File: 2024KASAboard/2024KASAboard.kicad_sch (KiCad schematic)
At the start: 2 parts, among them U1 Pico, U2 BME280

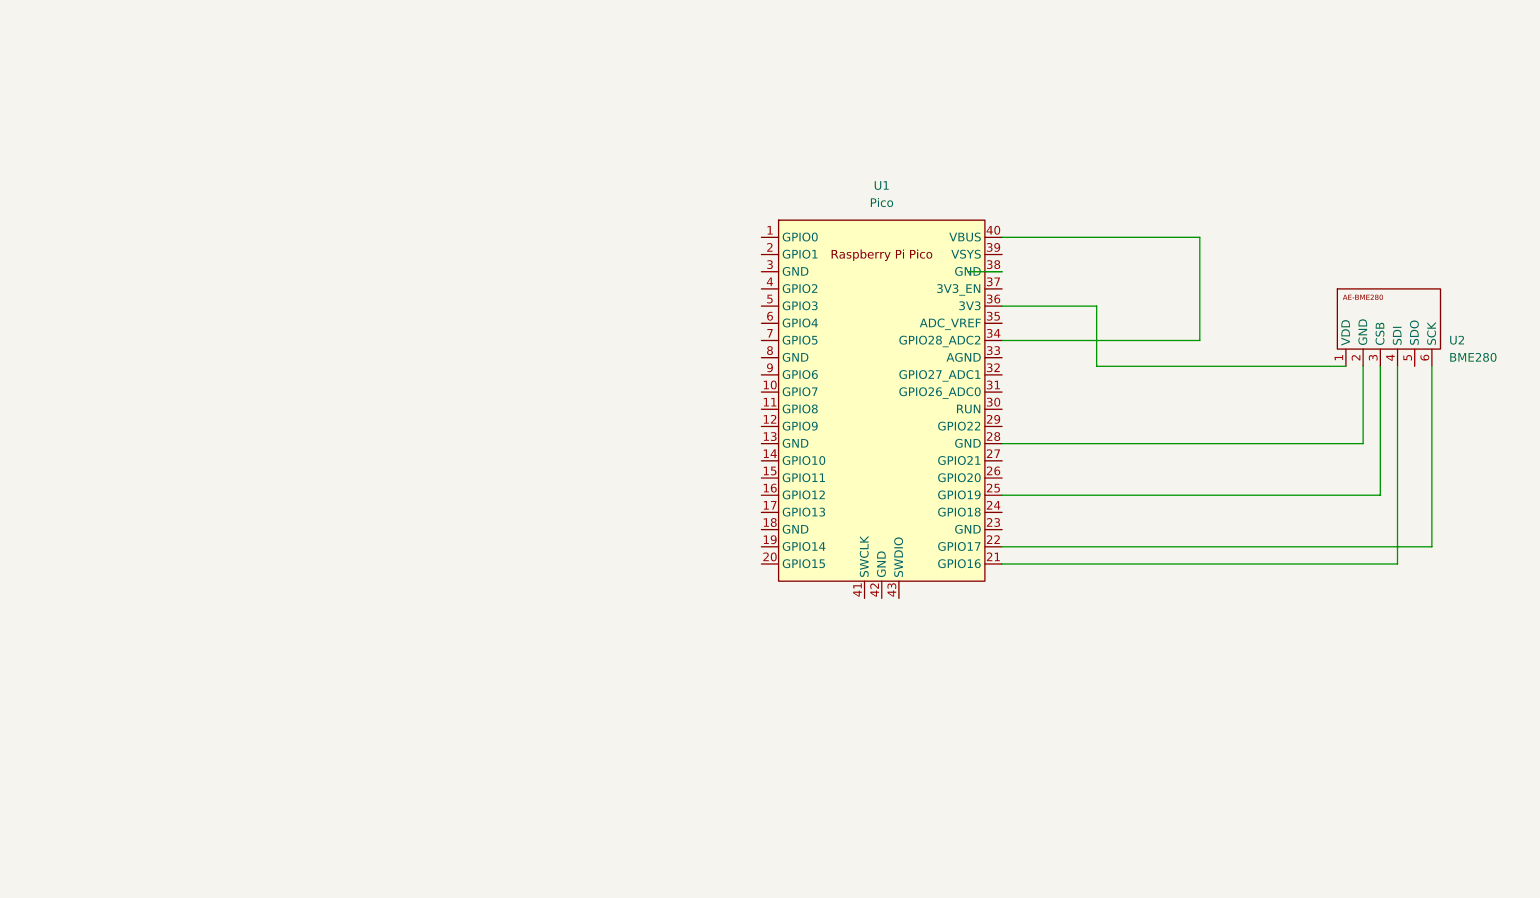
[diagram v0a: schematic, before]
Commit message: boardschcomp
回路図(基本)
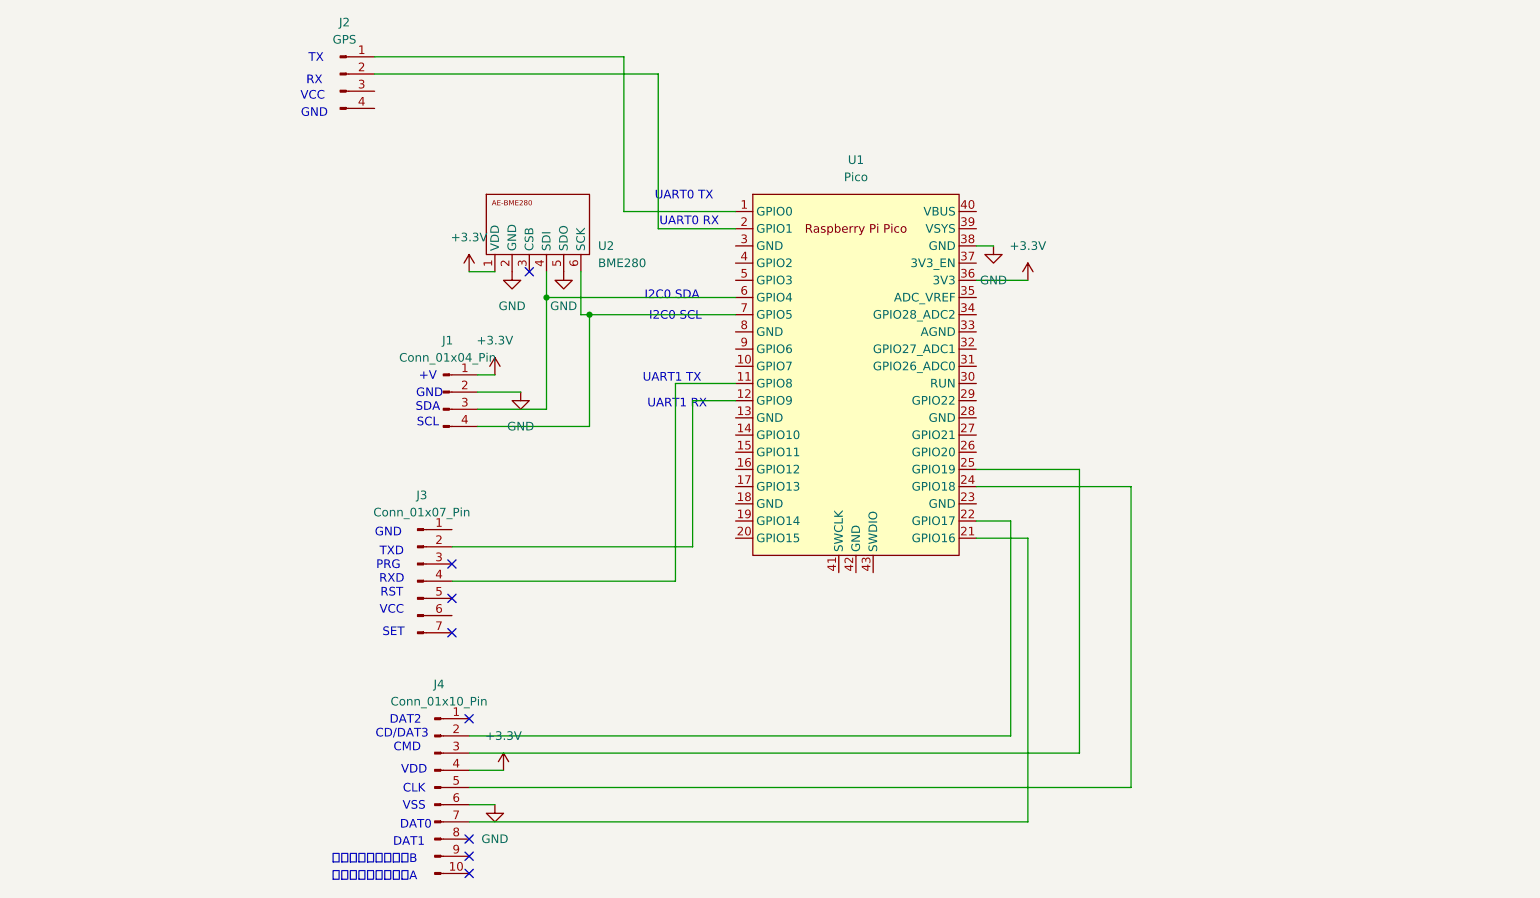
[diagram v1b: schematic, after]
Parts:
- added J1: Conn_01x04_Pin, symbol Connector:Conn_01x04_Pin
- added J2: GPS, symbol Connector:Conn_01x04_Pin
- added J3: Conn_01x07_Pin, symbol Connector:Conn_01x07_Pin
- added J4: Conn_01x10_Pin, symbol Connector:Conn_01x10_Pin
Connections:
- net +3.3V: now reaches U1.36 (3V3), U2.1 (VDD)
- net +3.3V: now also J1.1 (Pin_1), J4.4 (Pin_4)
- net at U1.28 (GND): no longer U2.2 (GND)
- net at U2.3 (CSB): no longer U1.25 (GPIO19)
- net at U2.4 (SDI): now also U1.6 (GPIO4), J1.3 (Pin_3); no longer U1.21 (GPIO16)
- net GND: now reaches U2.5 (SDO)
- net GND: now also U1.38 (GND), U2.2 (GND), J1.2 (Pin_2), J4.6 (Pin_6)
- net at U2.6 (SCK): now also U1.7 (GPIO5), J1.4 (Pin_4); no longer U1.22 (GPIO17)
- net at U1.1 (GPIO0): now also J2.1 (Pin_1)
- net at U1.11 (GPIO8): now also J3.4 (Pin_4)
- net at U1.12 (GPIO9): now also J3.2 (Pin_2)
- net at U1.2 (GPIO1): now also J2.2 (Pin_2)
- net at U1.24 (GPIO18): now also J4.5 (Pin_5)
- net at U1.34 (GPIO28_ADC2): no longer U1.40 (VBUS)
- new net: J4.2 (Pin_2), U1.22 (GPIO17)
- new net: J4.3 (Pin_3), U1.25 (GPIO19)
- new net: J4.7 (Pin_7), U1.21 (GPIO16)
- no-connect marks 0 -> 8
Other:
- note added: "+V"
- note added: "CD/DAT3"
- note added: "CLK"
- note added: "CMD"
- note added: "DAT0"
- note added: "DAT1"
- note added: "DAT2"
- note added: "GND"
- note added: "I2C0 SCL"
- note added: "I2C0 SDA"
- note added: "PRG"
- note added: "RST"
- note added: "RX"
- note added: "RXD"
- note added: "SCL"
- note added: "SDA"
- note added: "SET"
- note added: "TX"
- note added: "TXD"
- note added: "UART0 RX"
- note added: "UART0 TX"
- note added: "UART1 RX"
- note added: "UART1 TX"
- note added: "VCC"
- note added: "VDD"
- note added: "VSS"
- note added: "カード検出スイッチA"
- note added: "カード検出スイッチB"

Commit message: base_sch_addbatt
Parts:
- added BT1: Battery_Cell_NiMH_3.6V, symbol Device:Battery_Cell
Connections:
- net +3.3V: now also BT1.2 (-)
- net at U1.39 (VSYS): now also BT1.1 (+)
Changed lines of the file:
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@@
 	(paper "A4")
+	(junction
+		(at 157.48 66.04)
+		(diameter 0)
+		(color 0 0 0 0)
+	)
 	(junction
 		(at 86.36 68.58)
@@
 	(wire
 		(pts
+			(xy 170.18 64.77) (xy 170.18 66.04)
+		)
+		(stroke
+			(width 0)
+			(type default)
+		)
+	)
+	(wire
+		(pts
 			(xy 76.2 82.55) (xy 82.55 82.55)
 		)
@@
 	(wire
 		(pts
+			(xy 157.48 66.04) (xy 170.18 66.04)
+		)
+		(stroke
+			(width 0)
+			(type default)
+		)
+	)
+	(wire
+		(pts
 			(xy 97.79 33.02) (xy 60.96 33.02)
 		)
@@
 	(wire
 		(pts
+			(xy 170.18 57.15) (xy 149.86 57.15)
+		)
+		(stroke
+			(width 0)
+			(type default)
+		)
+	)
+	(wire
+		(pts
 			(xy 76.2 80.01) (xy 78.74 80.01)
 		)
@@
 		(pts
 			(xy 72.39 110.49) (xy 105.41 110.49)
+		)
+		(stroke
+			(width 0)
+			(type default)
+		)
+	)
+	(wire
+		(pts
+			(xy 149.86 57.15) (xy 149.86 58.42)
 		)
 		(stroke
@@
 					(unit 1)
 				)
+			)
+		)
+	)
+	(symbol
+		(lib_id "Device:Battery_Cell")
+		(at 170.18 62.23 0)
+		(unit 1)
+		(exclude_from_sim no)
+		(in_bom yes)
+		(on_board yes)
+		(dnp no)
+		(fields_autoplaced yes)
+		(property "Reference" "BT1"
+			(at 173.99 59.1184 0)
+			(effects
+				(font
+					(size 1.27 1.27)
+				)
+				(justify left)
+			)
+		)
+		(property "Value" "Battery_Cell_NiMH_3.6V"
+			(at 173.99 61.6584 0)
+			(effects
+				(font
+					(size 1.27 1.27)
+				)
+				(justify left)
+			)
+		)
+		(property "Footprint" ""
+			(at 170.18 60.706 90)
+			(effects
+				(font
+					(size 1.27 1.27)
+				)
+				(hide yes)
+			)
+		)
+		(property "Datasheet" "~"
+			(at 170.18 60.706 90)
+			(effects
+				(font
+					(size 1.27 1.27)
+				)
+				(hide yes)
+			)
+		)
+		(property "Description" "Single-cell battery"
+			(at 170.18 62.23 0)
+			(effects
+				(font
+					(size 1.27 1.27)
+				)
+				(hide yes)
+			)
+		)
+		(pin "2"
+		)
+		(pin "1"
+		)
+		(instances
+			(project ""
+				(path "/4d225088-d5b7-4ded-a7cf-f00dc9bc15f8"
+					(reference "BT1")
+					(unit 1)
+				)

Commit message: PCBdraft
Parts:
- removed J1: Conn_01x04_Pin, symbol Connector:Conn_01x04_Pin
- removed J3: Conn_01x07_Pin, symbol Connector:Conn_01x07_Pin
- added J1, J5: Conn_01x04_Socket, symbol Connector:Conn_01x04_Socket
- added J3: Conn_01x04_Pin, symbol Connector:Conn_01x04_Pin
- added U3: AE-GPS, symbol 0_kasa_lib-2024-:AE-GPS
- added U4: ~, symbol 0_kasa_lib-2024-:AE-LSM9DS1
- added U5: TWELITE-UART, symbol 0_kasa_lib-2024-:TWELITE-UART
- added U7: convunit, symbol 0_kasa_lib-2024-:convunit
- BT1: value Battery_Cell_NiMH_3.6V -> Battery_Cell
- J2: value GPS -> Conn_01x04_Pin
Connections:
- net +3.3V: now also J2.4 (Pin_4), J1.4 (Pin_4), U4.1 (+V), U5.6 (VCC), U7.3 (3.3V)
- net GND: now also J2.3 (Pin_3), J1.3 (Pin_3), U3.3 (GND), U4.2 (GND), U5.1 (GND), U7.2 (GND)
- net at U2.4 (SDI): now also J2.2 (Pin_2), U4.3 (SDA); no longer U1.6 (GPIO4)
- net at U2.6 (SCK): now also J2.1 (Pin_1), U4.4 (SCL); no longer U1.7 (GPIO5)
- net at U1.1 (GPIO0): now also J5.4 (Pin_4); no longer J2.1 (Pin_1)
- net at U1.2 (GPIO1): now also J5.3 (Pin_3); no longer J2.2 (Pin_2)
- net at U1.12 (GPIO9): now also J5.1 (Pin_1)
- net at U1.11 (GPIO8): now also J5.2 (Pin_2)
- new net: J3.1 (Pin_1), U5.2 (TXD)
- new net: J3.2 (Pin_2), U5.4 (RXD)
- new net: J3.3 (Pin_3), U3.1 (TXD)
- new net: J3.4 (Pin_4), U3.2 (RXD)
- new net: J1.1 (Pin_1), U1.7 (GPIO5)
- new net: J1.2 (Pin_2), U1.6 (GPIO4)
- new net: U3.4 (5V), U7.1 (5V)
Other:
- note removed: "+V"
- note removed: "GND"
- note removed: "PRG"
- note removed: "RST"
- note removed: "RX"
- note removed: "RXD"
- note removed: "SCL"
- note removed: "SDA"
- note removed: "SET"
- note removed: "TX"
- note removed: "TXD"
- note removed: "VCC"
- moved on the sheet: BT1, U2
